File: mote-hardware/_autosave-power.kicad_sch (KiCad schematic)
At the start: 6 parts, among them J1 USB_C_Receptacle_USB2.0_14P, U2 NCP1117-3.3_SOT223

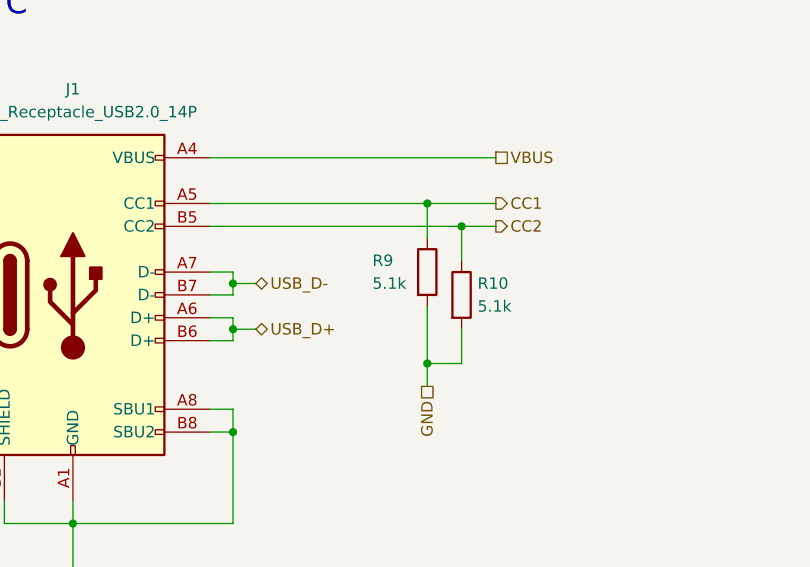
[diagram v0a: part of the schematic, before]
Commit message: Get pcb ready for first prototype order
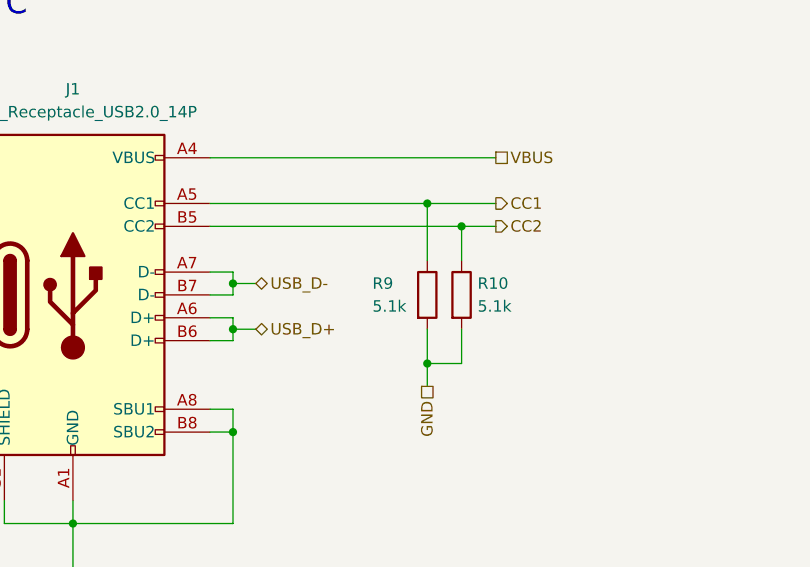
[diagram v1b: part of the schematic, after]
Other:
- moved on the sheet: R9
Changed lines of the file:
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@@
 	(wire
 		(pts
-			(xy 105.41 100.33) (xy 105.41 106.68)
+			(xy 105.41 102.87) (xy 105.41 106.68)
 		)
 		(stroke
@@
 	(wire
 		(pts
-			(xy 105.41 88.9) (xy 105.41 92.71)
+			(xy 105.41 88.9) (xy 105.41 95.25)
 		)
 		(stroke
@@
 	(symbol
 		(lib_id "Device:R")
-		(at 105.41 96.52 0)
+		(at 105.41 99.06 0)
 		(unit 1)
 		(exclude_from_sim no)
@@
 		(dnp no)
 		(property "Reference" "R9"
-			(at 99.314 95.25 0)
+			(at 99.314 97.79 0)
 			(effects
 				(font
@@
 		)
 		(property "Value" "5.1k"
-			(at 99.314 97.79 0)
+			(at 99.314 100.33 0)
 			(effects
 				(font
@@
 		)
 		(property "Footprint" "Resistor_SMD:R_0402_1005Metric"
-			(at 103.632 96.52 90)
+			(at 103.632 99.06 90)
 			(effects
 				(font
@@
 		)
 		(property "Datasheet" "~"
-			(at 105.41 96.52 0)
+			(at 105.41 99.06 0)
 			(effects
 				(font
@@
 		)
 		(property "Description" "Resistor"
-			(at 105.41 96.52 0)
-			(effects
-				(font
+			(at 105.41 99.06 0)
+			(effects
+				(font
